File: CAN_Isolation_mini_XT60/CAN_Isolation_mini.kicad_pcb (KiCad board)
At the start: 4 copper layers, 60 x 70 mm, 60 parts, among them J1 S4B-XH-A, J10 Conn_01x04_Pin, J11 Conn_01x04_Pin, J12 Conn_01x04_Pin, J13 Conn_01x04_Pin, J14 Conn_01x04_Pin, J15 Conn_01x04_Pin, J16 Conn_01x04_Pin, J17 Conn_01x04_Pin, J2 Conn_01x04_Pin, J21 XT60PW-F, J22 XT60PW-F, J3 Conn_01x04_Pin, J4 Conn_01x04_Pin, J5 Conn_01x04_Pin, J6 Conn_01x04_Pin, J7 Conn_01x04_Pin, J8 Conn_01x04_Pin, J9 Conn_01x04_Pin, U1 MCP2518FDT-H/SL, U2 ISO1042QDWVRQ1, U3 MGS3123R3, U4 MGS1R51205, U5 TVS1800DRVR, U6 DTC114ECAHZGT116, U7 MGS102405, Y1 CSTNE20M0V530000R0

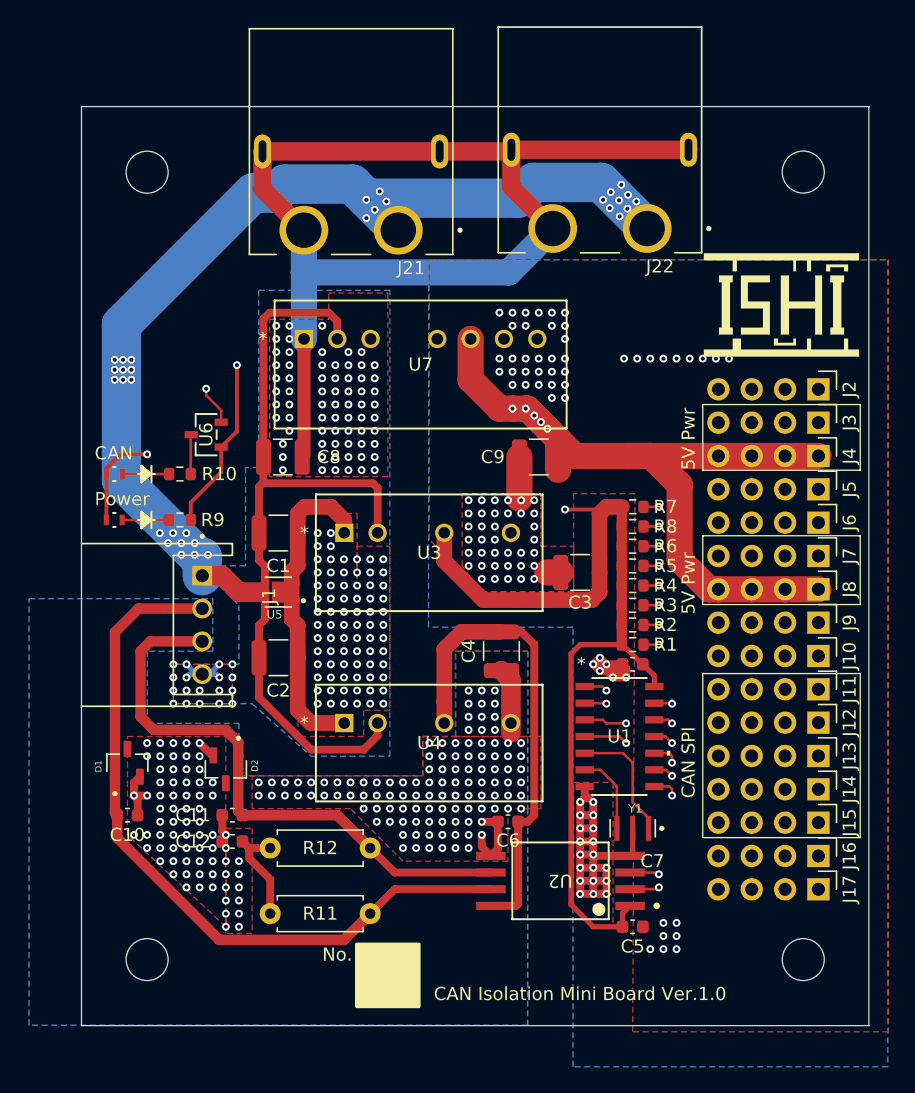
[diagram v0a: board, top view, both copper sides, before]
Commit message: Add diode for servo line.
Add diode for servo line.
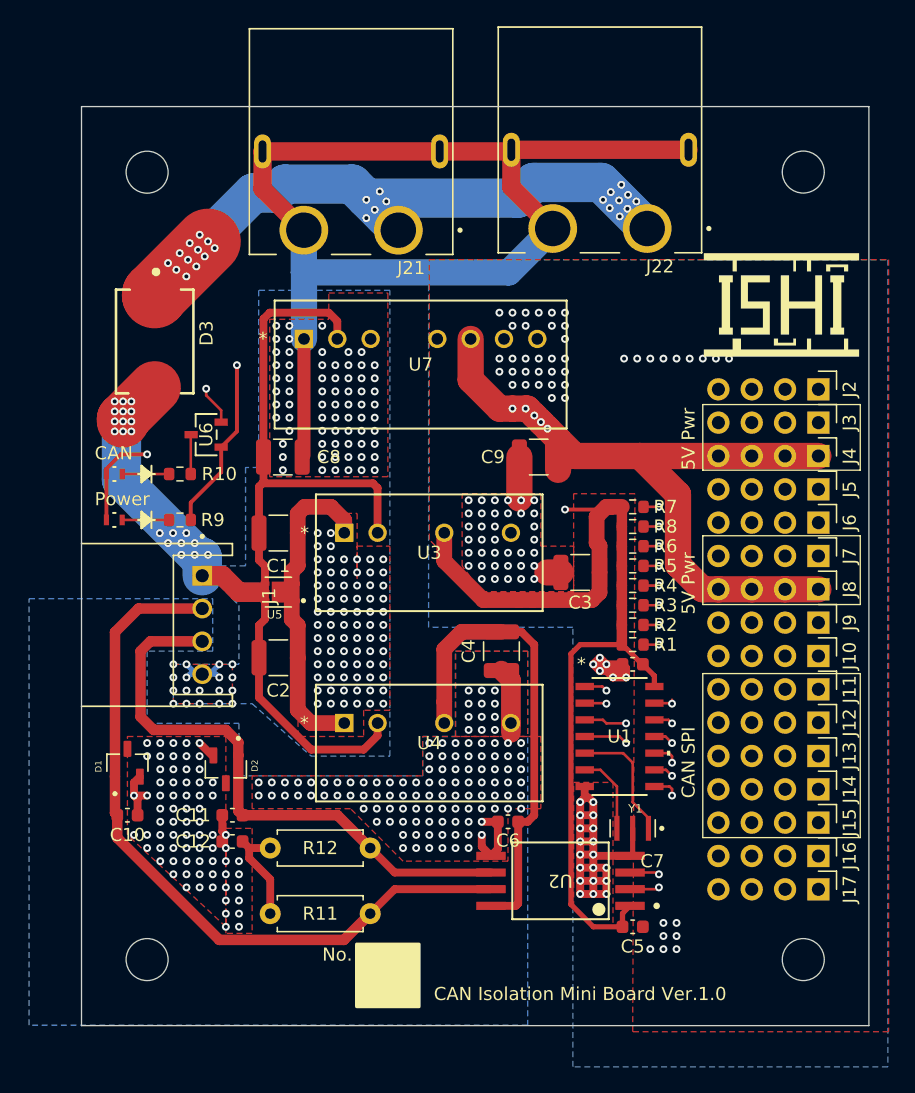
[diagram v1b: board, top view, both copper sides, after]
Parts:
- added D3: B520CQ-13-F, CAN_Isolation:DIOM7959X250N, F.Cu at (94.2, 75.7)
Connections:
- J21 pad 1: BAT_12V -> Net-(D3-PadC)
- J22 pad 1: BAT_12V -> Net-(D3-PadC)
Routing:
- net BAT_12V: track 283.6 -> 100.4 mm, vias 32 -> 21
- net Net-(D3-PadC): track 0.00 -> 139.9 mm, vias 0 -> 26
- net +5VP: track 109.8 -> 111.6 mm

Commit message: Change board size.
Change board size.
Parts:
- moved G*** 50.1 mm to (136.5, 122.7)
- moved REF** 10.0 mm to (143.7, 72.8)
- moved REF** 10.0 mm to (93.7, 72.8)
- moved J22 9.32 mm to (127.2, 76.4)
- moved J21 9.11 mm to (109.2, 76.3)
- moved U7 6.24 mm to (105.6, 81.7)
- moved C8 6.06 mm to (103.6, 90.6)
- moved D3 5.83 mm to (95.9, 81.3), turned to 180 degrees
- moved C9 5.50 mm to (129.0, 84.7)
- moved C1 4.60 mm to (103.7, 94.9)
- moved U5 4.60 mm to (103.7, 99.4)
- moved U6 3.91 mm to (99.4, 86.5)
- moved C11 3.51 mm to (100.2, 115.3)
- moved C12 3.51 mm to (100.2, 117.3)
- moved C2 3.51 mm to (103.7, 103.3)
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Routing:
- net BAT_GND: track 149.9 -> 113.2 mm, vias 163 -> 167
- net BAT_12V: track 100.4 -> 118.0 mm, vias 21 -> 25
- net Net-(D3-PadC): track 139.9 -> 125.7 mm, vias 26 -> 16
- net CAN_LED: track 93.3 -> 106.2 mm
- net GND_VP: track 89.3 -> 95.9 mm, vias 109 -> 107
- net CAN_L: track 44.7 -> 48.2 mm
- net +3.3VP: track 132.1 -> 135.5 mm
- net GND_5VCAN: track 18.2 -> 21.4 mm, vias 186 -> 183
- net CAN_SCK: track 31.7 -> 29.7 mm
- net CAN_SDI: track 27.0 -> 25.6 mm
- net CAN_H: track 56.4 -> 57.9 mm
- net Net-(R10-Pad2): track 3.01 -> 1.78 mm
- net +5VP: track 111.6 -> 112.7 mm
- net Net-(LED2-Pad1): track 3.57 -> 4.37 mm
- net CAN_SDO: track 23.2 -> 22.6 mm
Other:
- board size 60 x 70 mm -> 60 x 60 mm

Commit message: Fix XT60 line.
Fix XT60 line.
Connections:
- J22 pad 1: Net-(D3-PadC) -> BAT_12V
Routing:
- net BAT_12V: track 118.0 -> 210.2 mm
- net Net-(D3-PadC): track 125.7 -> 64.3 mm
- net +5VP: track 112.7 -> 110.7 mm
- net BAT_GND: vias 167 -> 166

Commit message: Change connector.
Change connector.
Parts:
- added X1: B2PS-VH, CAN_Isolation:B2PS-VH, F.Cu at (97.9, 95.9)
- J1: value S4B-XH-A -> S2B-XH-A; footprint CAN_Isolation:JST_S4B-XH-A -> CAN_Isolation:JST_S2B-XH-A
- moved J1 7.86 mm to (92.0, 105.2)
- moved D1 3.79 mm to (92.0, 111.6)
- moved C10 3.32 mm to (91.9, 115.1)
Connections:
- J1 pad 1: BAT_12V -> CAN_H
- J1 pad 2: CAN_H -> CAN_L
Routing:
- net CAN_L: track 48.2 -> 32.1 mm
- net GND_5VCAN: track 21.4 -> 27.4 mm, vias 183 -> 180
- net CAN_H: track 57.9 -> 52.5 mm
- net +5VP: track 110.7 -> 108.6 mm
- net BAT_GND: vias 166 -> 171
